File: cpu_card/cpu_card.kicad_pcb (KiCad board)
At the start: 4 copper layers, 90.2 x 95.8 mm, 71 parts, among them J101 PC/104 ISA, J103 80188, J104 256K ROM, J201 22V10/16V8, J203 ~{RESET}, J204 ISPEXT, J301 UART1, J302 UART2, J303 USB B, SW201 RESET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

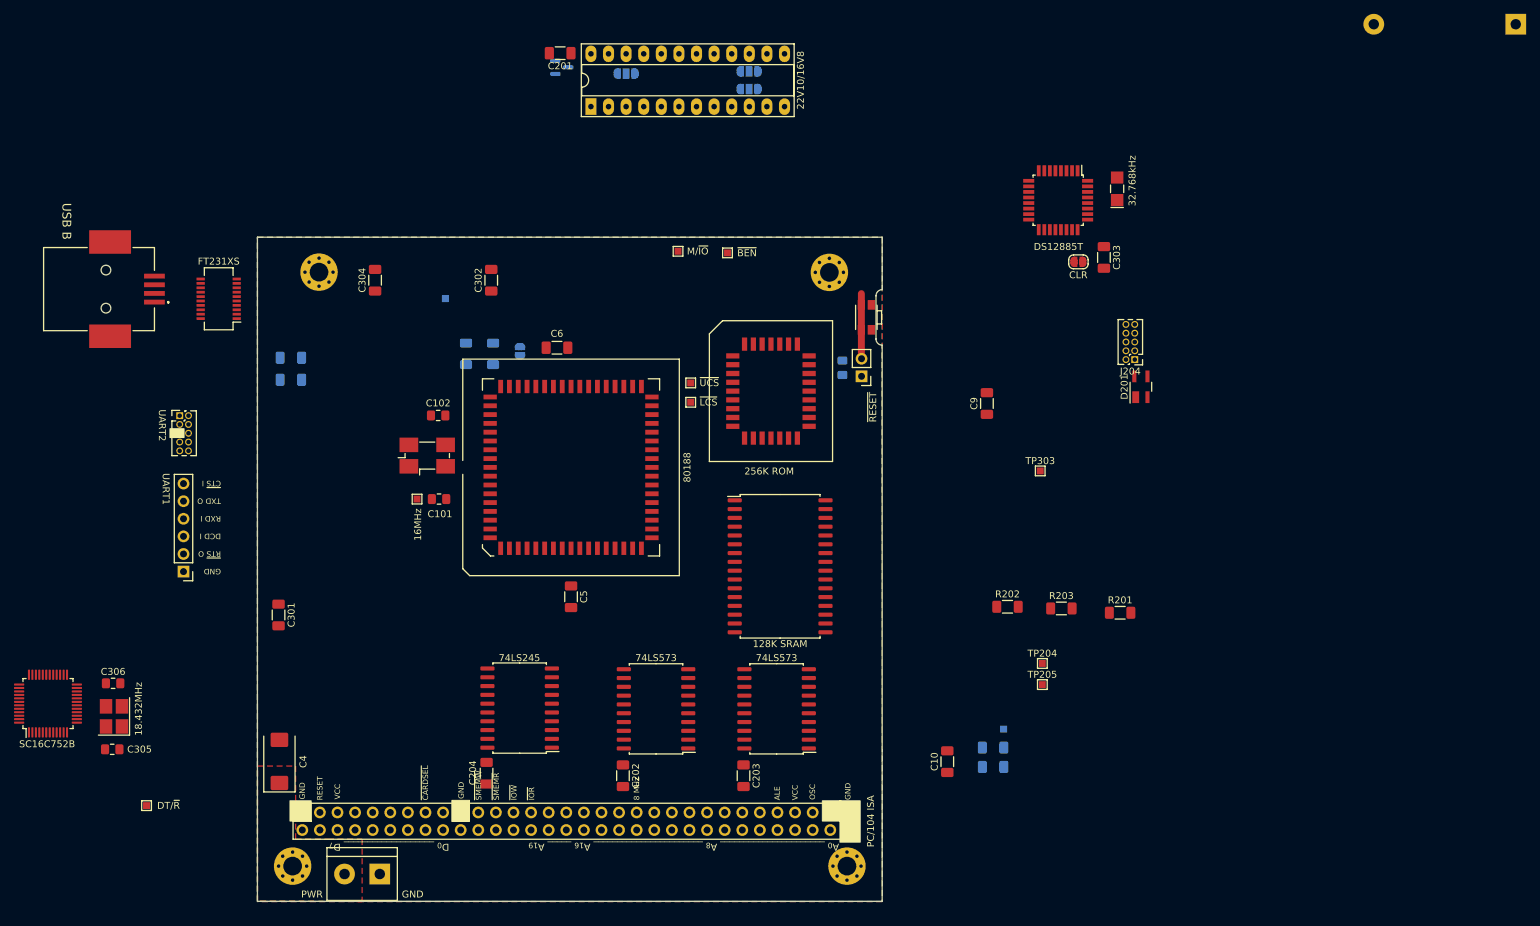
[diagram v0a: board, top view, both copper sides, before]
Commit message: bios library and overall cleanup
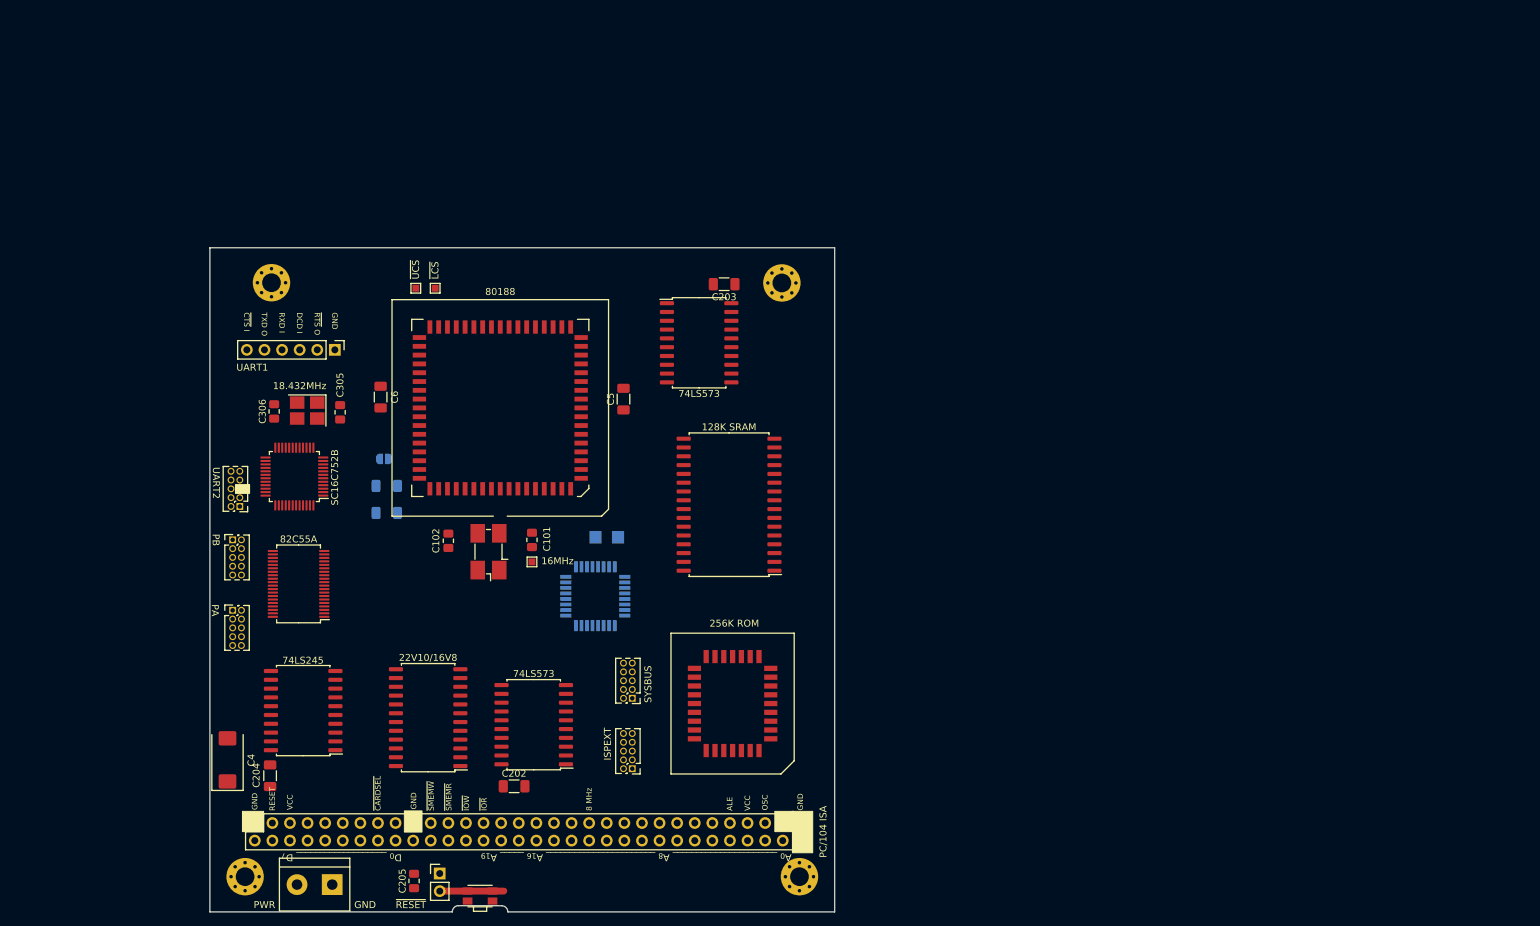
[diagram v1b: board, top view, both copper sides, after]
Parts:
- removed BT301: RTC Battery, Battery:BatteryHolder_Keystone_106_1x20mm
- removed C10, C201, C301, C302, C303, C304, C9: 100n/0.1u PWR, Capacitor_SMD:C_1206_3216Metric_Pad1.33x1.80mm_HandSolder
- removed D201: BAS28, Package_TO_SOT_SMD:SOT-143_Handsoldering
- removed J303: USB B, A-USB_B_SMT:AUSBBSMT
- removed JP201: GND DCD, Jumper:SolderJumper-3_P1.3mm_Open_RoundedPad1.0x1.5mm
- removed JP202: ~{OE} USB.~{RESET}, Jumper:SolderJumper-3_P1.3mm_Open_RoundedPad1.0x1.5mm
- removed JP203: SERIAL, Jumper:SolderJumper-3_P1.3mm_Open_RoundedPad1.0x1.5mm
- removed R1: TMR1 >, Resistor_SMD:R_1206_3216Metric_Pad1.30x1.75mm_HandSolder
- removed R201, R203: PullUp, Resistor_SMD:R_1206_3216Metric_Pad1.30x1.75mm_HandSolder
- removed R202: PullDown, Resistor_SMD:R_1206_3216Metric_Pad1.30x1.75mm_HandSolder
- removed R302: R4k7, Resistor_SMD:R_1206_3216Metric_Pad1.30x1.75mm_HandSolder
- removed R303: R10k, Resistor_SMD:R_1206_3216Metric_Pad1.30x1.75mm_HandSolder
- removed R4: TMR0 >, Resistor_SMD:R_1206_3216Metric_Pad1.30x1.75mm_HandSolder
- removed SW301: CLR, Jumper:SolderJumper-2_P1.3mm_Open_RoundedPad1.0x1.5mm
- removed TP102: TMR1 >, TestPoint:TestPoint_Pad_1.0x1.0mm
- removed TP201: M/~{IO}, TestPoint:TestPoint_Pad_1.0x1.0mm
- removed TP202: DT/~{R}, TestPoint:TestPoint_Pad_1.0x1.0mm
- removed TP203: ~{BEN}, TestPoint:TestPoint_Pad_1.0x1.0mm
- removed TP204: ~{WR}, TestPoint:TestPoint_Pad_1.0x1.0mm
- removed TP205: ~{RD}, TestPoint:TestPoint_Pad_1.0x1.0mm
- removed TP302: CBUS1, TestPoint:TestPoint_Pad_1.0x1.0mm
- removed TP303: CBUS2, TestPoint:TestPoint_Pad_1.0x1.0mm
- removed U204: TLV809EA45DBZR, Package_TO_SOT_SMD:SOT-23
- removed U302: FT231XS, Package_SO:SSOP-20_3.9x8.7mm_P0.635mm
- added J102: SYSBUS, Connector_PinHeader_1.27mm:PinHeader_2x05_P1.27mm_Vertical, F.Cu at (149.5, 119.9)
- added J304: PB, Connector_PinHeader_1.27mm:PinHeader_2x05_P1.27mm_Vertical, F.Cu at (91.8, 97.0)
- added J305: PA, Connector_PinHeader_1.27mm:PinHeader_2x05_P1.27mm_Vertical, F.Cu at (91.8, 107.2)
- added U304: 82C55A, Package_SO:TSSOP-40_6.1x11mm_P0.5mm, F.Cu at (101.3, 103.4)
- C205: moved to F.Cu
- J201: footprint Package_DIP:DIP-24_W7.62mm_Socket_LongPads -> Package_SO:SOIC-24W_7.5x15.4mm_P1.27mm
- U303, Y302: moved to B.Cu
- moved SW201 100.4 mm to (127.5, 148.4), turned to 0 degrees
- moved C205 96.5 mm to (118.0, 146.3), turned to 90 degrees
- moved J203 94.1 mm to (121.7, 145.2), turned to 0 degrees
- moved J204 93.5 mm to (149.5, 130.0)
- moved J201 91.3 mm to (120.0, 122.7), turned to 180 degrees
- moved Y302 89.2 mm to (145.8, 96.6), turned to 0 degrees
- moved U303 87.9 mm to (144.1, 105.2), turned to 180 degrees
- moved C203 71.0 mm to (162.7, 60.1), turned to 180 degrees
- moved C305 58.7 mm to (107.3, 78.6), turned to -90 degrees
- moved U201 54.0 mm to (159.1, 68.6), turned to 0 degrees
- moved Y301 52.2 mm to (102.6, 78.4), turned to 180 degrees
- moved U301 48.4 mm to (100.7, 87.9), turned to 180 degrees
- moved C306 45.6 mm to (97.8, 78.5), turned to 90 degrees
- moved J104 45.4 mm to (164.0, 120.7), turned to 180 degrees
- moved TP103 42.0 mm to (118.2, 60.7), turned to -90 degrees
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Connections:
- J103 pad 28: unconnected-(J103-Pad28) -> ~{PCS2}
- J103 pad 46: GND -> NMI
- J103 pad 51: HLDA -> unconnected-(J103-Pad51)
- J201 pad 10: 16V8.GND -> DCD
- J201 pad 15: 16V8.~{OE} -> USB.~{RESET}
- J201 pad 22: Net-(J201-Pad22) -> ~{CS_S1}
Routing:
- removed copper zone on B.Cu, net GND
- removed copper zone on F.Cu, net GND
- removed copper zone on In1.Cu, net GND
- removed copper zone on In2.Cu, net GND
- removed copper zone on F.Cu, net VCC
- removed copper zone on In1.Cu, net VCC
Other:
- board size 90.2 x 95.8 mm -> 90.2 x 95.9 mm
